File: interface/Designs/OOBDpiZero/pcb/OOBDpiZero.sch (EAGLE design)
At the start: 133 parts, among them IC1 LM1117MPX-3.3, IC11 EEPROM24, IC3 DS3231, Q2 12MHz, U1 SN65HVD230(SO8), U2 SN65HVD230(SO8), U3 MAX98357, U4 SY6280, U5 MP1482

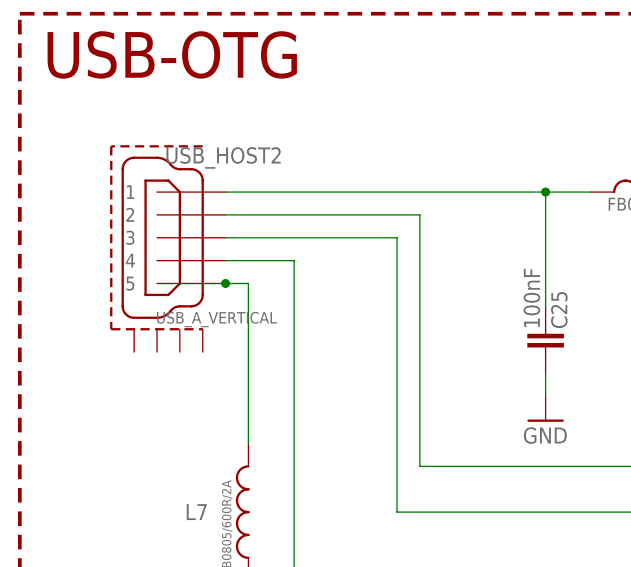
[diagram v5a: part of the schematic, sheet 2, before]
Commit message: 7 Lines left over, error checking in regards of overlap, distance and restriction done. Mike, please check the restrictions in regards of e.g mounting holes of the pizero pcb
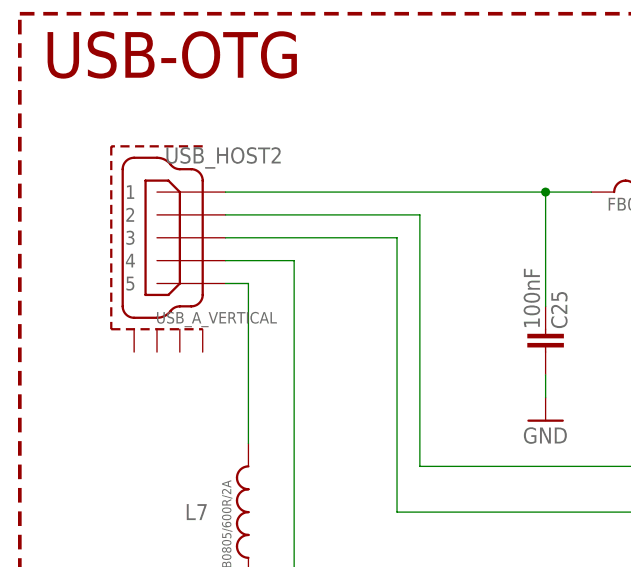
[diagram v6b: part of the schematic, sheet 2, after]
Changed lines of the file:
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@@
 <?xml version="1.0" encoding="utf-8"?>
 <!DOCTYPE eagle SYSTEM "eagle.dtd">
-<eagle version="7.2.0">
+<eagle version="7.6.0">
 <drawing>
 <settings>
@@
 <setting verticaltext="up"/>
 </settings>
-<grid distance="50" unitdist="mil" unit="mil" style="lines" multiple="1" display="yes" altdistance="0.01" altunitdist="inch" altunit="inch"/>
+<grid distance="0.1" unitdist="inch" unit="inch" style="lines" multiple="1" display="no" altdistance="0.01" altunitdist="inch" altunit="inch"/>
 <layers>
 <layer number="1" name="Top" color="4" fill="1" visible="no" active="no"/>
@@
 </segment>
 </net>
-<net name="N$49" class="0">
-<segment>
-<pinref part="USB_HOST2" gate="G$1" pin="5"/>
-<pinref part="USB_HOST2" gate="G$1" pin="5"/>
-<wire x1="30.48" y1="142.24" x2="33.02" y2="142.24" width="0.1524" layer="91"/>
-<wire x1="33.02" y1="142.24" x2="33.02" y2="124.46" width="0.1524" layer="91"/>
-<pinref part="L7" gate="G$1" pin="2"/>
-<junction x="30.48" y="142.24"/>
-</segment>
-</net>
 <net name="USB2_DM" class="0">
 <segment>
@@
 </segment>
 </net>
+<net name="N$44" class="0">
+<segment>
+<pinref part="USB_HOST2" gate="G$1" pin="5"/>
+<pinref part="USB_HOST2" gate="G$1" pin="5"/>
+<pinref part="L7" gate="G$1" pin="2"/>
+<wire x1="30.48" y1="142.24" x2="33.02" y2="142.24" width="0.1524" layer="91"/>
+<wire x1="33.02" y1="142.24" x2="33.02" y2="124.46" width="0.1524" layer="91"/>
+</segment>
+</net>

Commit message: add minor modifications after schematics review
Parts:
- removed R11, R4: NI, rcl:R-EU_R0603
- added JP3: 3V3 power (opt), jumper:JP1E
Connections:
- new net N$50: C32.1, IC1.OUT, IC1.OUT1, JP3.2
- net +3V3: now also JP3.1, R12.2, R5.2; no longer C32.1, IC1.OUT, IC1.OUT1
- net GND: no longer R12.2, R5.2
- net HS-CAN_RS: no longer R4.2
- net MS-CAN_RS: no longer R11.2
- net N$5: now also U$3.PC13; no longer R4.1
- net N$80: now also U$2.PC13; no longer R11.1
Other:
- note added: "= 9dB GAIN"
- moved on the sheet: PP22, PP23, R12, R5

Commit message: start modifications on wire width to a default of 10mil modify all via to octagon instead of mixture for round a square
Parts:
- removed C45, C46: 220pF, rcl:C-EUC0603K
- removed C47: 1uF, rcl:C-EUC0603
- removed C50: 100nF, rcl:C-EUC0603
- removed C51: 10nF, rcl:C-EUC0603
- removed C53, C54, C55, C56: 22uF/6.3V, rcl:C-EUC0603
- removed C57, C59: 100nF, resistor:C-EUC0603
- removed C58, C60: 22uF/6.3V, rcl:CPOL-EUSMCA
- removed D3: SMBJ16A, OLIMEX_DISCRET:SMBJ16A
- removed IC11: EEPROM24, FLYFISH:EEPROM24
- removed L7: FB0805/600R/2A, rcl:L-USL0603
- removed R26: 1M, resistor:R-EU_R0603
- removed R27: 680R, resistor:R-EU_R0603
- removed R28, R32: 10k, rcl:R-EU_R0603
- removed R30, R31: NI(0R), resistor:R-EU_R0603
- removed R33: 10k, resistor:R-EU_R0603
- removed R34: NI(0R), resistor:R-EU_R0805
- removed R37: 4.99k/1%, rcl:R-EU_R0603
- removed R39: 2.2k/1%, rcl:R-EU_R0603
- removed R52, R53: NI, resistor:R-EU_R0603
- removed U3: MAX98357, microbuilder:AUDIOAMP_MAX98357
- removed U5: MP1482, OLIMEX_IC:MP1482
- added C100, C104: 22uF/6.3V, rcl:C-EUC0603
- added C102, C105, C33, C35: 100nF, rcl:C-EUC0603K
- added C103, C107: NI (10nF), resistor:C-EUC0603
- added C106, C108, C109, C110, C111: 100nF, resistor:C-EUC0603
- added D101: PESD1CAN, Industrialberry:PESD1CAN
- added IC100: LM1117MPX-3.3, lm1117:LM1117MPX-3.3
- added L100: FB0805/600R/2A, rcl:L-USL0603
- added R104, R115: 330R, rcl:R-EU_R0603
- added R106, R113: 10k, rcl:R-EU_R0603
- added R108: 6k8k/1%, rcl:R-EU_R0603
- added R109, R110, R111, R112, R114, R116: 60R, resistor:R-EU_R0603
- added R11: 10k, resistor:R-EU_R0603
- added U101, U102: SN65HVD230(SO8), arm:MCP2551
- C1, C30: value 100nF -> 10uF/6.3V; device rcl:C-EUC0603K -> rcl:C-EUC0603
- C10, C18: value 100nF -> 22uF/6.3V; device resistor:C-EUC0603 -> rcl:CPOL-EUSMCA
- C11, C22, C25: device rcl:C-EUC0603K -> resistor:C-EUC0603
- C12: value 100nF -> 1uF
- C13: value 100nF -> 33pF
- C14: value NI (10nF) -> 10uF; device resistor:C-EUC0603 -> rcl:C-EUC0805K
- C15, C20: value 100nF -> 220pF; device resistor:C-EUC0603 -> rcl:C-EUC0603K; MANEX (none) -> 123-0001115
- C17: value 33pF -> 100nF
- C2: device resistor:C-EUC0603 -> rcl:C-EUC0603
- C21: value 1uF -> 100nF
- C23: device rcl:C-EUC0603 -> rcl:C-EUC0603K
- C26: value 22uF/6.3V -> 100nF; device rcl:C-EUC0603 -> resistor:C-EUC0603
- C27: value 22uF/6.3V -> 100nF
- C28: value 22uF/6.3V -> 1uF
- C3: value NI (10nF) -> 100nF
- C31: value 10uF/6.3V -> 22uF/6.3V
- C32: value 10uF/6.3V -> 10nF
- C4: value 10uF -> 22uF/6.3V; device rcl:C-EUC0805K -> rcl:C-EUC0603
- C5, C6, C7: value 100nF -> 22uF/6.3V; device resistor:C-EUC0603 -> rcl:C-EUC0603
- D1: value PESD1CAN -> SMBJ16A; device Industrialberry:PESD1CAN -> OLIMEX_DISCRET:SMBJ16A
- IC1: value LM1117MPX-3.3 -> EEPROM24; device lm1117:LM1117MPX-3.3 -> FLYFISH:EEPROM24
- JP1: value Audio-Out -> 3V3 power (opt); device jumper:JP1Q -> jumper:JP1E
- JP2: value Prog0_IO -> UART; device jumper:JP4E -> jumper:JP2E
- JP3: value 3V3 power (opt) -> Audio-Out; device jumper:JP1E -> jumper:JP1Q
- JP4: value UART -> Prog0_IO; device jumper:JP2E -> jumper:JP4E
- R10, R3: value 60R -> 330R; device resistor:R-EU_R0603 -> rcl:R-EU_R0603
- R12: value 10k -> 2.2k/1%
- R13, R17: value 330R -> NI; device rcl:R-EU_R0603 -> resistor:R-EU_R0603; MANEX (none) -> 110-0002014
- R14: value 330R -> 10k; device rcl:R-EU_R0603 -> resistor:R-EU_R0603
- R16: value 60R -> 10k
- R2, R9: value 60R -> 10k; device resistor:R-EU_R0603 -> rcl:R-EU_R0603
- R20: value 330R -> NI(0R); device rcl:R-EU_R0603 -> resistor:R-EU_R0603
- R21: value 10k -> NI(0R); device resistor:R-EU_R0603 -> resistor:R-EU_R0805
- R22: value 10k -> NI(0R)
- R23: value NA(47k) -> 10k; device resistor:R-EU_R0603 -> rcl:R-EU_R0603
- R24: value 6k8k/1% -> 10k
- R25: value 10k -> 4.99k/1%
- R5: value 10k -> 680R; device rcl:R-EU_R0603 -> resistor:R-EU_R0603
- R6: value 10k -> 330R
- R7: value 60R -> NA(47k)
- R8: value 330R -> 1M; device rcl:R-EU_R0603 -> resistor:R-EU_R0603; MANEX (none) -> 110-0002014
- U1: value SN65HVD230(SO8) -> MAX98357; device arm:MCP2551 -> microbuilder:AUDIOAMP_MAX98357
- U2: value SN65HVD230(SO8) -> MP1482; device arm:MCP2551 -> OLIMEX_IC:MP1482
- renumbered BAT1 to BAT100, C48 to C101, C52 to C34, D2 to D100, IC3 to IC2, L6 to L2, LED3 to LED103, LED4 to LED102, LED5 to LED104, LED6 to LED101, LED7 to LED1, LED8 to LED100, PP22 to PP1, PP23 to PP2, Q2 to Q1, R29 to R4, R35 to R102, R36 to R101, R41 to R105, R42 to R107, R43 to R103, R44 to R100, U$2 to U$102, U$3 to U$100, U$5 to U$101, U4 to U100, USB_HOST2 to USB_HOST100
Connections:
- net +12V: now also D1.C, R24.1, U2.IN; no longer D3.C, R32.1, U5.IN
- net +3V3: now also C105.1, C106.2, C108.2, C109.2, C111.2, C19.2, C24.1, C25.2, C26.2, C28.2, C3.2, JP1.1, JP4.1, R104.1, R106.2, R113.2, R115.1, R2.1, R23.1, U101.VDD, U102.VDD; no longer C10.2, C11.1, C12.2, C13.2, C2.2, C22.1, C47.2, C5.2, C6.2, C7.2, C8.2, JP2.1, JP3.1, R1.1, R12.2, R15.1, R20.1, R5.2, R6.1, U1.VDD, U2.VDD
- net +5V: now also C102.1, C14.1, C18.+, C2.2, C22.1, C23.1, C5.1, C6.1, C7.1, IC1.VCC, IC100.IN, R1.1, R11.1, R12.1, R17.2, R21.2, R25.2, R8.2, R9.1, U1.VDD; no longer C1.1, C23.2, C31.1, C53.1, C54.1, C55.1, C56.1, C59.1, C60.+, IC1.IN, IC11.VCC, R22.1, R25.1, R26.2, R28.1, R34.2, R37.2, R39.1, R53.2, U3.VDD
- net AUD_BCLK: now also U1.BCLK; no longer U3.BCLK
- net AUD_DIN: now also U1.DIN; no longer U3.DIN
- net AUD_LRCLK: now also U1.LRCLK; no longer U3.LRCLK
- net AUD_SD_MODE: now also R8.1, U1.!SD_MODE; no longer R26.1, U3.!SD_MODE
- net GND: now also C10.-, C100.2, C102.2, C103.2, C104.2, C105.2, C106.1, C107.2, C108.1, C109.1, C110.1, C111.1, C12.2, C13.2, C18.-, C19.1, C20.1, C21.1, C23.2, C25.1, C26.1, C28.1, C3.1, C33.2, C35.2, C5.2, C6.2, C7.2, C8.2, C9.2, D1.A, D101.CC, IC1.A0, IC1.A1, IC1.A2, IC100.GND, JP2.3, JP4.4, L100.1, R108.1, R112.2, R116.2, R13.1, R5.1, R7.1, U1.GND, U101.VSS, U102.VSS, U2.GND; no longer C10.1, C12.1, C13.1, C18.2, C19.2, C20.2, C21.2, C23.1, C25.2, C26.2, C28.2, C3.2, C32.2, C45.1, C46.1, C47.1, C5.1, C50.2, C53.2, C54.2, C55.2, C56.2, C57.2, C58.-, C59.2, C6.1, C60.-, C7.1, C8.1, C9.1, D1.CC, D3.A, IC11.A0, IC11.A1, IC11.A2, IC11.GND, JP2.4, JP4.3, L7.1, R16.2, R23.1, R24.1, R27.1, R52.1, R7.2, U1.VSS, U2.VSS, U3.GND, U5.GND
- net HS-CAN_H: now also D101.C2, R111.2, U102.CANH; no longer D1.C2, R2.2, U1.CANH
- net HS-CAN_L: now also D101.C1, U102.CANL; no longer D1.C1, U1.CANL
- net HS-CAN_RXD: now also U102.RXD; no longer U1.RXD
- net HS-CAN_TXD: now also U102.TXD; no longer U1.TXD
- net ID_SC: now also IC1.SCL; no longer IC11.SCL
- net ID_SD: now also IC1.SDA, R9.2; no longer IC11.SDA, R25.2
- net MS-CAN_H: now also R109.2, U101.CANH; no longer R9.2, U2.CANH
- net MS-CAN_L: now also U101.CANL; no longer U2.CANL
- net MS-CAN_RXD: now also U101.RXD; no longer U2.RXD
- net MS-CAN_TXD: now also U101.TXD; no longer U2.TXD
- net N$1: now also C31.1, L4.1, R21.1; no longer C27.1, L5.1, R34.1
- net N$10: now also C103.1, R109.1, R110.1; no longer C14.1, R10.1, R9.1
- net N$12: now also C20.2, JP3.1, U1.OUTP; no longer C46.2, JP1.1, U3.OUTP
- net N$129: now also R12.2; no longer R39.2
- net N$13: now also R6.2; no longer R8.2
- net N$14: now also R10.2; no longer R13.2
- net N$15: now also R112.1; no longer R7.1
- net N$16: now also R3.2; no longer R14.2
- net N$17: now also R3.1; no longer R14.1
- net N$18: now also R10.1; no longer R13.1
- net N$19: now also R6.1; no longer R8.1
- net N$2: now also C107.1, R111.1, R114.1; no longer C3.1, R2.1, R3.1
- net N$20: now also C110.2, R104.2; no longer C9.2, R15.2
- net N$21: now also R116.1; no longer R16.1
- net N$22: now also R15.2; no longer R17.2
- net N$27: now also R15.1; no longer R17.1
- net N$28: now also C21.2, R115.2; no longer C15.2, R20.2
- net N$29: now also C16.1; no longer C17.1
- net N$3: now also C15.2, JP3.2, U1.OUTN; no longer C45.2, JP1.2, U3.OUTN
- net N$30: now also R114.2; no longer R3.2
- net N$31: now also C13.1; no longer C16.1
- net N$32: now also R110.2; no longer R10.2
- net N$33: now also C10.+, C17.1, R14.2, R16.2; no longer C57.1, C58.+, R21.2, R33.2
- net N$34: now also R14.1; no longer R33.1
- net N$35: now also R16.1; no longer R21.1
- net N$36: now also C12.1, R11.2, R7.2; no longer C21.1, R22.2, R23.2
- net N$37: now also R13.2, R17.1, U1.GAIN; no longer R52.2, R53.1, U3.GAIN
- net N$38: now also R22.1; no longer R30.1
- net N$39: now also C11.1, C8.1, C9.1; no longer C18.1, C19.1, C20.1
- net N$4: now also C27.1, U2.SS; no longer C50.1, U5.SS
- net N$40: now also R5.2; no longer R27.2
- net N$41: now also C33.1, L5.2; no longer C24.1, L4.2
- net N$42: now also L100.2; no longer L3.2
- net N$43: now also R20.1; no longer R31.1
- net N$44: now also L3.2; no longer L7.2
- net N$45: now also R108.2; no longer R24.2
- net N$46: now also IC1.WP, R1.2; no longer IC11.WP, R28.2
- net N$47: now also C100.1, C104.1, L5.1; no longer C26.1, C28.1, L4.1
- net N$48: now also C35.1, L4.2; no longer C25.1, L5.2
- net N$5: now also R113.1, U102.RS; no longer R5.1, U1.RS
- net N$50: now also C1.1, IC100.OUT, IC100.OUT1, JP1.2; no longer C32.1, IC1.OUT, IC1.OUT1, JP3.2
- net N$6: now also R24.2, U2.EN; no longer R32.2, U5.EN
- net N$62: now also R25.1, U2.FB; no longer R37.1, U5.FB
- net N$7: now also C32.1, U2.BS; no longer C51.1, U5.BS
- net N$8: now also C32.2, U2.SW; no longer C51.2, U5.SW
- net N$80: now also R106.1, U101.RS; no longer R12.1, U2.RS
- net N$9: now also U2.COMP; no longer U5.COMP
- net PP22: now also R20.2; no longer R31.2
- net PP23: now also R22.2; no longer R30.2
- net SCL: now also R23.2; no longer R1.2
- net SDA: now also R2.2; no longer R6.2
- net SWCLK: now also JP4.3; no longer JP2.3
- net SWDIO: now also JP4.2; no longer JP2.2
- net UART0_RXD: now also JP2.2; no longer JP4.2
- net UART0_TXD: now also JP2.1; no longer JP4.1
